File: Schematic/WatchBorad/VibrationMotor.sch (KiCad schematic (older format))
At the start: 7 parts

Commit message: Added PowerSupply and MCU hierarchical sheets.
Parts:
- M?: footprint MotorsLocalLib:4x4x11 -> LocalFootprints:VibrationMorot4x4x11
- TP?: footprint (none) -> testpoints:testpoint
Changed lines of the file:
@@
 $Descr A4 11693 8268
 encoding utf-8
-Sheet 2 2
+Sheet 2 4
 Title ""
 Date ""
@@
 F 0 "M?" H 7400 3025 50  0000 L CNN
 F 1 "Motor_DC" V 7425 2825 50  0001 L CNN
-F 2 "MotorsLocalLib:4x4x11" H 7250 2985 50  0001 C CNN
+F 2 "LocalFootprints:VibrationMorot4x4x11" H 7250 2985 50  0001 C CNN
 F 3 "https://www.aliexpress.com/item/32844746278.html?spm=a2g0o.productlist.0.0.24ef228a6Cfn5S&algo_pvid=3165a7c1-ba73-4c2c-bb27-6dacea1bed25&algo_expid=3165a7c1-ba73-4c2c-bb27-6dacea1bed25-0&btsid=0b8b15c915866028623212205ec781&ws_ab_test=searchweb0_0,searchweb201602_,searchweb201603_" H 7250 2985 50  0001 C CNN
 	1    7250 3075
@@
 F 0 "TP?" H 6208 3772 50  0000 L CNN
 F 1 "TestPoint" H 6208 3727 50  0001 L CNN
-F 2 "" H 6350 3700 50  0001 C CNN
+F 2 "testpoints:testpoint" H 6350 3700 50  0001 C CNN
 F 3 "~" H 6350 3700 50  0001 C CNN
 	1    6150 3700

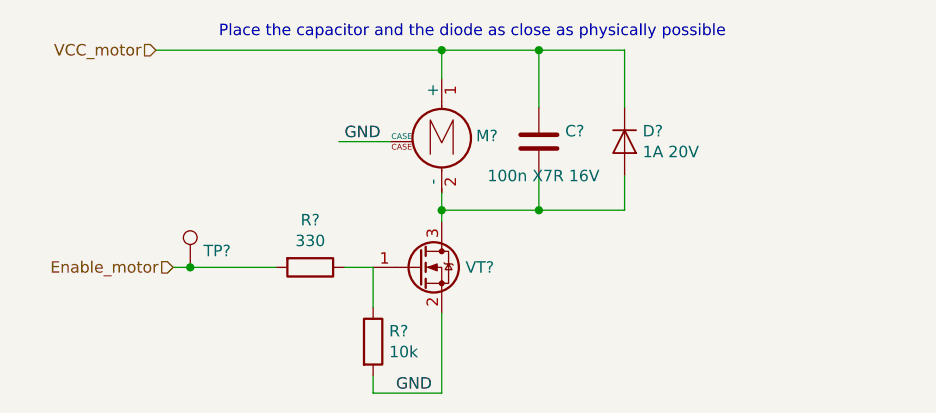
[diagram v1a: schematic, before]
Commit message: Added on/off circuit for PON and added other changes
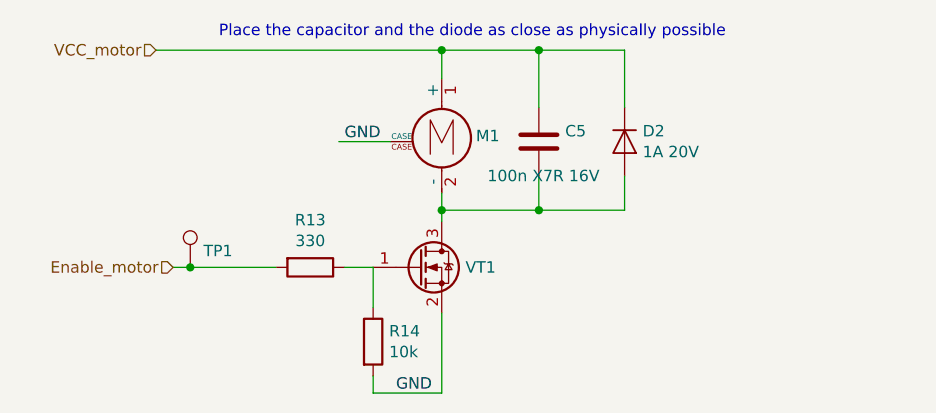
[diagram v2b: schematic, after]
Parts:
- gave numbers to parts that had none: 7
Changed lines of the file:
@@
 $Descr A4 11693 8268
 encoding utf-8
-Sheet 2 4
+Sheet 2 5
 Title ""
 Date ""
@@
 $EndDescr
 $Comp
-L MotorLocal:Motor_DC M?
+L MotorLocal:Motor_DC M1
 U 1 1 5E9679A5
 P 7250 3075
-F 0 "M?" H 7400 3025 50  0000 L CNN
+F 0 "M1" H 7400 3025 50  0000 L CNN
 F 1 "Motor_DC" V 7425 2825 50  0001 L CNN
 F 2 "LocalFootprints:VibrationMorot4x4x11" H 7250 2985 50  0001 C CNN
@@
 VCC_motor
 $Comp
-L MosfetLocal:SL2300 VT?
+L MosfetLocal:SL2300 VT1
 U 1 1 5E950239
 P 7225 3700
-F 0 "VT?" H 7354 3700 50  0000 L CNN
+F 0 "VT1" H 7354 3700 50  0000 L CNN
 F 1 "SL2300" H 7355 3655 50  0001 L CNN
 F 2 "TO_SOT_Packages_SMD:SOT-23" H 7225 3700 50  0001 C CNN
@@
 	7250 3375 7250 3450
 $Comp
-L Device:R R?
+L Device:R R14
 U 1 1 5E95D4D2
 P 6950 4025
-F 0 "R?" H 7020 4071 50  0000 L CNN
+F 0 "R14" H 7020 4071 50  0000 L CNN
 F 1 "10k" H 7020 3980 50  0000 L CNN
 F 2 "Resistors_SMD:R_0603_HandSoldering" V 6880 4025 50  0001 C CNN
@@
 $EndComp
 $Comp
-L Device:R R?
+L Device:R R13
 U 1 1 5E95E60A
 P 6675 3700
-F 0 "R?" V 6468 3700 50  0000 C CNN
+F 0 "R13" V 6468 3700 50  0000 C CNN
 F 1 "330" V 6559 3700 50  0000 C CNN
 F 2 "Resistors_SMD:R_0603_HandSoldering" V 6605 3700 50  0001 C CNN
@@
 	7250 2750 6000 2750
 $Comp
-L Connector:TestPoint TP?
+L Connector:TestPoint TP1
 U 1 1 5E966959
 P 6150 3700
-F 0 "TP?" H 6208 3772 50  0000 L CNN
+F 0 "TP1" H 6208 3772 50  0000 L CNN
 F 1 "TestPoint" H 6208 3727 50  0001 L CNN
 F 2 "testpoints:testpoint" H 6350 3700 50  0001 C CNN
@@
 Place the capacitor and the diode as close as physically possible
 $Comp
-L Device:C C?
+L Device:C C5
 U 1 1 5E969686
 P 7675 3150
-F 0 "C?" H 7790 3196 50  0000 L CNN
+F 0 "C5" H 7790 3196 50  0000 L CNN
 F 1 "100n X7R 16V" H 7450 3000 50  0000 L CNN
 F 2 "Capacitors_SMD:C_0603_HandSoldering" H 7713 3000 50  0001 C CNN
@@
 $EndComp
 $Comp
-L Device:D D?
+L Device:D D2
 U 1 1 5E96AA9C
 P 8050 3150
-F 0 "D?" V 8004 3229 50  0000 L CNN
+F 0 "D2" V 8004 3229 50  0000 L CNN
 F 1 "1A 20V" V 8095 3229 50  0000 L CNN
 F 2 "Diodes_SMD:D_SMA_Handsoldering" H 8050 3150 50  0001 C CNN
